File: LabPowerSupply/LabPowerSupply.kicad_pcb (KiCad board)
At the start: 4 copper layers, 203 parts, among them Q1_CP1 FMMT495TA, Q1_CP2 FMMT495TA, Q1_LVR1 PJA3404_R1_00001, Q1_LVR2 PJA3404_R1_00001, Q2_LVR1 PJA3404_R1_00001, Q2_LVR2 PJA3404_R1_00001, Q3_LVR1 PJA3404_R1_00001, Q3_LVR2 PJA3404_R1_00001, Y1 8M, Y2 8M

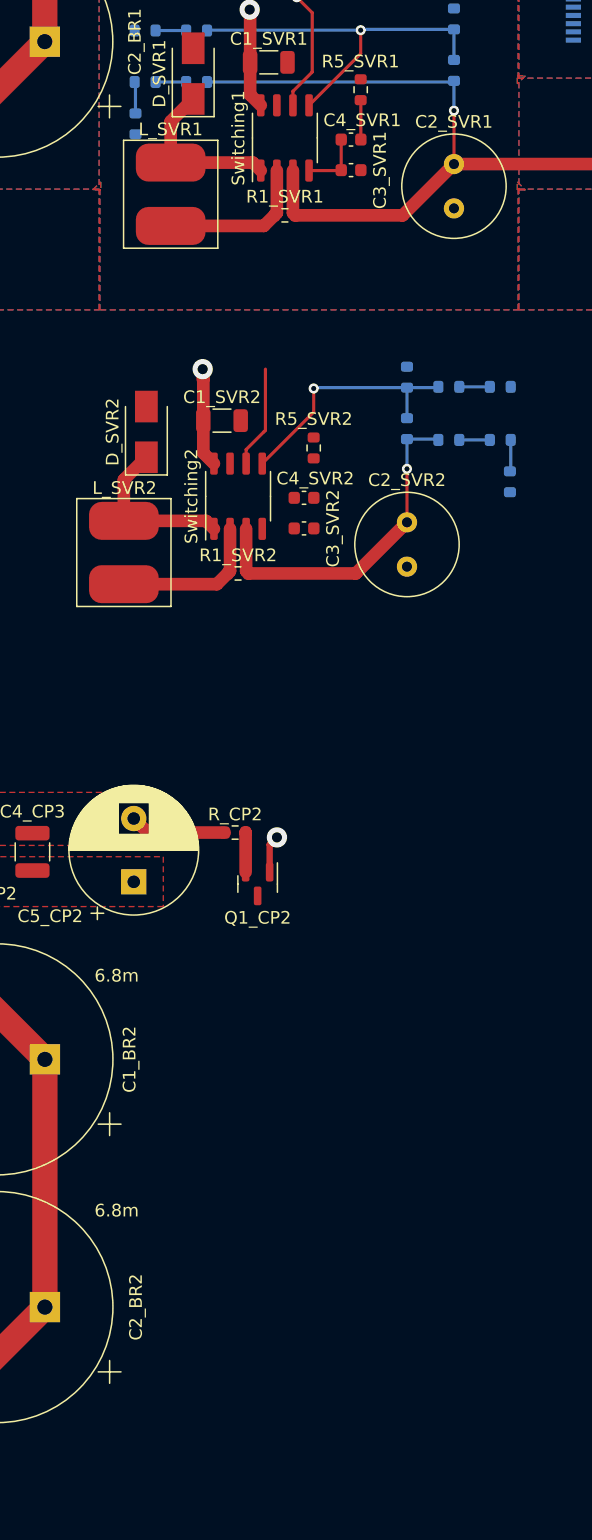
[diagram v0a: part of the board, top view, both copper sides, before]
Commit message: Copied channel module positions other than linear
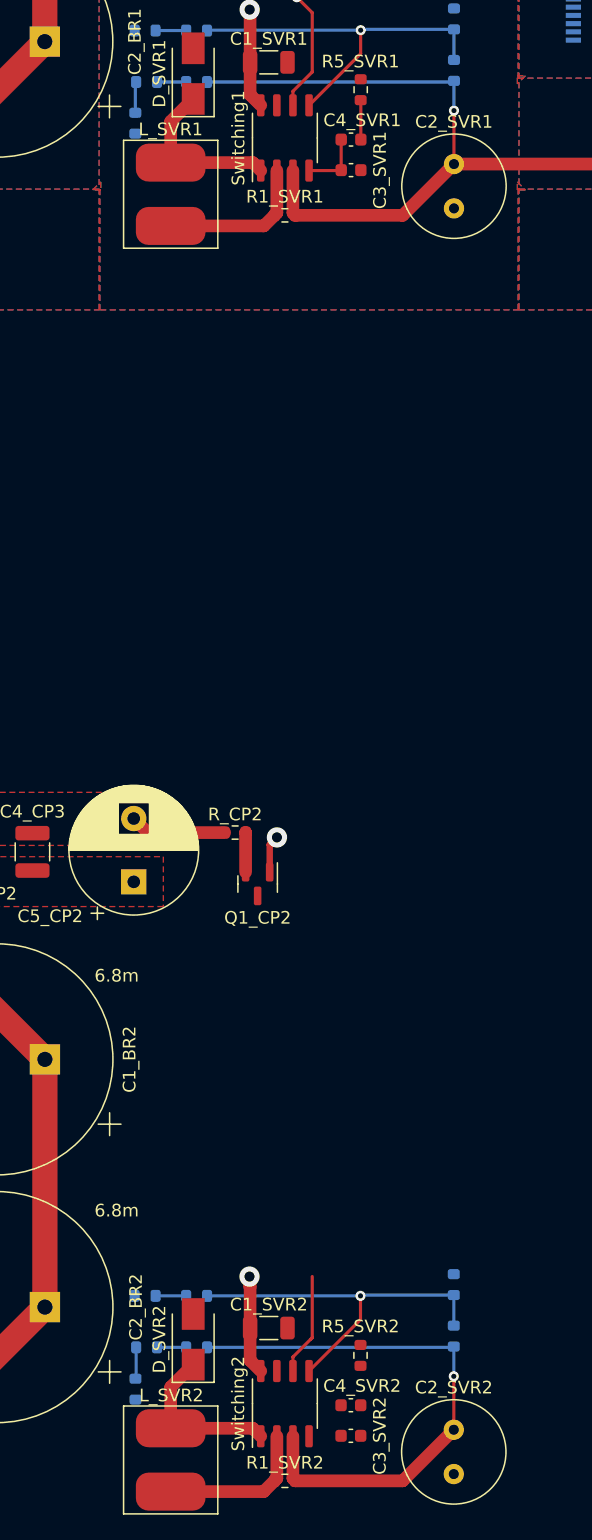
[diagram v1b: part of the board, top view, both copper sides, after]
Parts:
- moved R6_SVR2 77.5 mm to (57.2, 173.5)
- moved R41_SVR2 77.1 mm to (57.9, 166.1), turned to 180 degrees
- moved R32_SVR2 76.9 mm to (58.0, 170.2), turned to 180 degrees
- moved R42_SVR2 74.5 mm to (62.0, 166.1), turned to 180 degrees
- moved R31_SVR2 74.4 mm to (62.0, 170.2), turned to 180 degrees
- moved C1_SVR2 71.7 mm to (67.7, 168.7)
- moved C4_SVR2 71.7 mm to (74.2, 174.8)
- moved R1_SVR2 71.7 mm to (69.0, 180.7)
- moved R7_SVR2 71.7 mm to (82.3, 165.2)
- moved C2_SVR2 71.7 mm to (82.3, 176.7)
- moved C3_SVR2 71.7 mm to (74.2, 177.2)
- moved L_SVR2 71.7 mm to (59.9, 179.1)
- moved R2_SVR2 71.7 mm to (82.3, 169.3)
- moved R5_SVR2 71.7 mm to (74.9, 170.8)
- moved Switching2 71.7 mm to (69.0, 174.6)
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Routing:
- net /Channel Power Supply 2/Linear Voltage Regulator /Linear Input: track 26.9 -> 43.9 mm
- net /Channel Power Supply 2/Switching Voltage Regulator/FeedBack: track 19.9 -> 29.5 mm

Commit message: Started mcu
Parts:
- moved C10_Power1 169.5 mm to (169.2, 34.4), turned to 90 degrees
- moved C2_Y1 166.6 mm to (185.9, 53.9), turned to 90 degrees
- moved C5_Power1 166.5 mm to (172.1, 34.4), turned to 90 degrees
- moved R11_OA2 163.1 mm to (80.4, 154.8)
- moved R12_OA2 163.1 mm to (64.3, 154.8)
- moved R13_OA2 163.1 mm to (63.5, 158.1)
- moved R2_OA2 163.1 mm to (64.3, 152.3)
- moved R51_OA2 163.1 mm to (69.9, 145.9)
- moved OpAmp2 163.1 mm to (72.3, 153.5)
- moved R10_OA2 163.1 mm to (82.2, 139.3)
- moved R4_OA2 163.1 mm to (74.6, 146.7)
- moved R52_OA2 163.1 mm to (69.0, 142.1)
- moved R6_OA2 163.1 mm to (65.0, 142.1)
- moved R7_OA2 163.1 mm to (78.4, 150.1)
- moved R8_OA2 163.1 mm to (75.5, 143.4)
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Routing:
- net +3.3V: track 4.22 -> 45.8 mm
- net GND1: track 17.5 -> 57.7 mm
- net Net-(C1_Y1-Pad2): track 0.00 -> 18.6 mm
- net Net-(C2_Y1-Pad2): track 0.00 -> 11.0 mm
- net Net-(J_Boot1-Pad2): track 0.00 -> 10.3 mm
- net Net-(J_Boot1-Pad1): track 0.00 -> 4.21 mm
- net Net-(J_Boot1-Pad3): track 0.00 -> 3.69 mm

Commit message: Fixed MCU communication pins and optocoupler
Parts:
- added R_I2C1: 4.7k, Resistor_SMD:R_0603_1608Metric, B.Cu at (199.9, 34.8)
- added R_I2C2: 4.7k, Resistor_SMD:R_0603_1608Metric, B.Cu at (199.9, 32.3)
- added R_OPT1: 470, Resistor_SMD:R_0603_1608Metric, F.Cu at (337.4, 30.2)
- added R_OPT2: 470, Resistor_SMD:R_0603_1608Metric, F.Cu at (329.4, 30.2)
- added R_OPT3: 10k, Resistor_SMD:R_0603_1608Metric, F.Cu at (329.4, 27.7)
- added R_OPT4: 10k, Resistor_SMD:R_0603_1608Metric, F.Cu at (337.4, 27.7)
- added R_OPT5: 10k, Resistor_SMD:R_0603_1608Metric, F.Cu at (333.4, 27.7)
- added R_OPT6: 10k, Resistor_SMD:R_0603_1608Metric, F.Cu at (333.4, 30.2)
- added R_USB1: 22, Resistor_SMD:R_0603_1608Metric, B.Cu at (270.3, 22.9)
- added R_USB2: 22, Resistor_SMD:R_0603_1608Metric, B.Cu at (270.3, 20.1)
- J_STLink1: value Conn_01x05_Male -> Conn_01x06_Male; footprint Connector_PinHeader_2.54mm:PinHeader_1x05_P2.54mm_Vertical -> Connector_PinHeader_2.54mm:PinHeader_1x06_P2.54mm_Vertical
- R_CC1, R_CC2: value 4.7k -> 5.1k
- moved D_LVR2 177.4 mm to (94.2, 144.1), turned to 180 degrees
- moved R4_LVR2 175.5 mm to (102.9, 67.6)
- moved C3_LVR2 175.4 mm to (101.5, 156.0), turned to -90 degrees
- moved Q3_LVR2 172.3 mm to (104.0, 161.3)
- moved Linear1_2 171.5 mm to (109.3, 142.0)
- moved Linear2 171.5 mm to (105.9, 155.9)
- moved C1_LVR2 171.3 mm to (117.7, 145.8), turned to 180 degrees
- moved R3_LVR2 170.5 mm to (98.6, 155.8)
- moved C4_LVR2 170.3 mm to (103.1, 142.7), turned to 180 degrees
- moved R13_LVR2 167.6 mm to (102.1, 171.6), turned to 0 degrees
- moved Inverter2 164.9 mm to (95.2, 165.0)
- moved R12_LVR2 163.0 mm to (107.1, 145.7)
- moved Q1_LVR2 161.5 mm to (94.8, 149.4), turned to 180 degrees
- moved Q2_LVR2 161.5 mm to (99.6, 149.6)
- moved R11_LVR2 160.0 mm to (103.1, 145.7)
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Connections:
- net /Primary Controller/Reset renamed Net-(MCU_1-Pad7)
- Front_Panel1 pad 1: +3.3V -> GND1
- Front_Panel1 pad 15: Net-(Front_Panel1-Pad15) -> GND1
- Front_Panel1 pad 2: Net-(Front_Panel1-Pad2) -> unconnected-(Front_Panel1-Pad2)
- Front_Panel1 pad 3: Net-(Front_Panel1-Pad3) -> Net-(MCU_1-Pad25)
- Front_Panel1 pad 4: Net-(Front_Panel1-Pad4) -> Net-(MCU_1-Pad26)
- Front_Panel1 pad 5: GND1 -> Net-(MCU_1-Pad27)
- Front_Panel1 pad 7: Net-(Front_Panel1-Pad7) -> Net-(MCU_1-Pad29)
- Inverter2 pad 3: Net-(Inverter2-Pad3) -> (no net)
- Inverter2 pad 4: /Optocouplers/RX 2 -> (no net)
- Inverter2 pad 5: /Optocouplers/TX 2 -> (no net)
- Inverter2 pad 6: Net-(Inverter2-Pad6) -> (no net)
- J_STLink1 pad 2: GND1 -> /Primary Controller/SW_CLK
- J_STLink1 pad 3: /Primary Controller/SWDIO -> GND1
- J_STLink1 pad 4: /Primary Controller/SWCLK -> /Primary Controller/SW_DIO
- MCU_1 pad 25: unconnected-(MCU_1-Pad25) -> Net-(MCU_1-Pad25)
- MCU_1 pad 26: Net-(Front_Panel1-Pad2) -> Net-(MCU_1-Pad26)
- MCU_1 pad 27: Net-(Front_Panel1-Pad3) -> Net-(MCU_1-Pad27)
- MCU_1 pad 28: Net-(Front_Panel1-Pad4) -> Net-(Front_Panel1-Pad6)
- MCU_1 pad 29: Net-(Front_Panel1-Pad16) -> Net-(MCU_1-Pad29)
- MCU_1 pad 30: Net-(Front_Panel1-Pad15) -> Net-(Front_Panel1-Pad8)
- MCU_1 pad 33: Net-(Front_Panel1-Pad14) -> Net-(Front_Panel1-Pad9)
- MCU_1 pad 34: Net-(Front_Panel1-Pad13) -> Net-(Front_Panel1-Pad10)
- MCU_1 pad 35: Net-(Front_Panel1-Pad12) -> Net-(Front_Panel1-Pad11)
- MCU_1 pad 37: Net-(Front_Panel1-Pad11) -> Net-(Front_Panel1-Pad12)
- MCU_1 pad 38: Net-(Front_Panel1-Pad10) -> Net-(Front_Panel1-Pad13)
- MCU_1 pad 39: Net-(Front_Panel1-Pad9) -> Net-(Front_Panel1-Pad14)
- MCU_1 pad 40: Net-(Front_Panel1-Pad8) -> Net-(Front_Panel1-Pad16)
- MCU_1 pad 44: Net-(J_USB1-PadA7) -> Net-(MCU_1-Pad44)
- MCU_1 pad 45: Net-(J_USB1-PadA6) -> Net-(MCU_1-Pad45)
- MCU_1 pad 46: /Primary Controller/SWDIO -> /Primary Controller/SW_DIO
- MCU_1 pad 49: /Primary Controller/SWCLK -> /Primary Controller/SW_CLK
- MCU_1 pad 55: Net-(Front_Panel1-Pad6) -> /Primary Controller/SWO
- MCU_1 pad 56: Net-(Front_Panel1-Pad7) -> unconnected-(MCU_1-Pad56)
- Optocoupler1 pad 2: /Optocouplers/TX1 -> Net-(Optocoupler1-Pad2)
- Optocoupler1 pad 3: GND1 -> /Optocouplers/TX1
- Optocoupler1 pad 6: Net-(Inverter2-Pad3) -> /Optocouplers/RX 2
- Optocoupler2 pad 2: Net-(Inverter2-Pad6) -> Net-(Optocoupler2-Pad2)
- Optocoupler2 pad 3: GND2 -> /Optocouplers/TX 2
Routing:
- net Net-(J_USB1-PadA1): track 0.00 -> 19.6 mm
- net /Primary Controller/I2C SDA: track 0.00 -> 17.2 mm
- net /Primary Controller/I2C SCL: track 0.00 -> 16.2 mm
- net GND1: track 57.7 -> 69.4 mm
- net +3.3V: track 45.8 -> 36.0 mm
- net /Primary Controller/SW_CLK: track 0.00 -> 9.33 mm
- net Net-(J_Boot1-Pad2): track 10.3 -> 17.7 mm
- net Net-(J_USB1-PadA5): track 0.00 -> 4.72 mm
- net Net-(J_USB1-PadB5): track 0.00 -> 4.22 mm
- net /Primary Controller/SWO: track 0.00 -> 4.15 mm
- net Net-(J_USB1-PadA7): track 0.00 -> 3.79 mm
- net Net-(J_USB1-PadA6): track 0.00 -> 3.79 mm

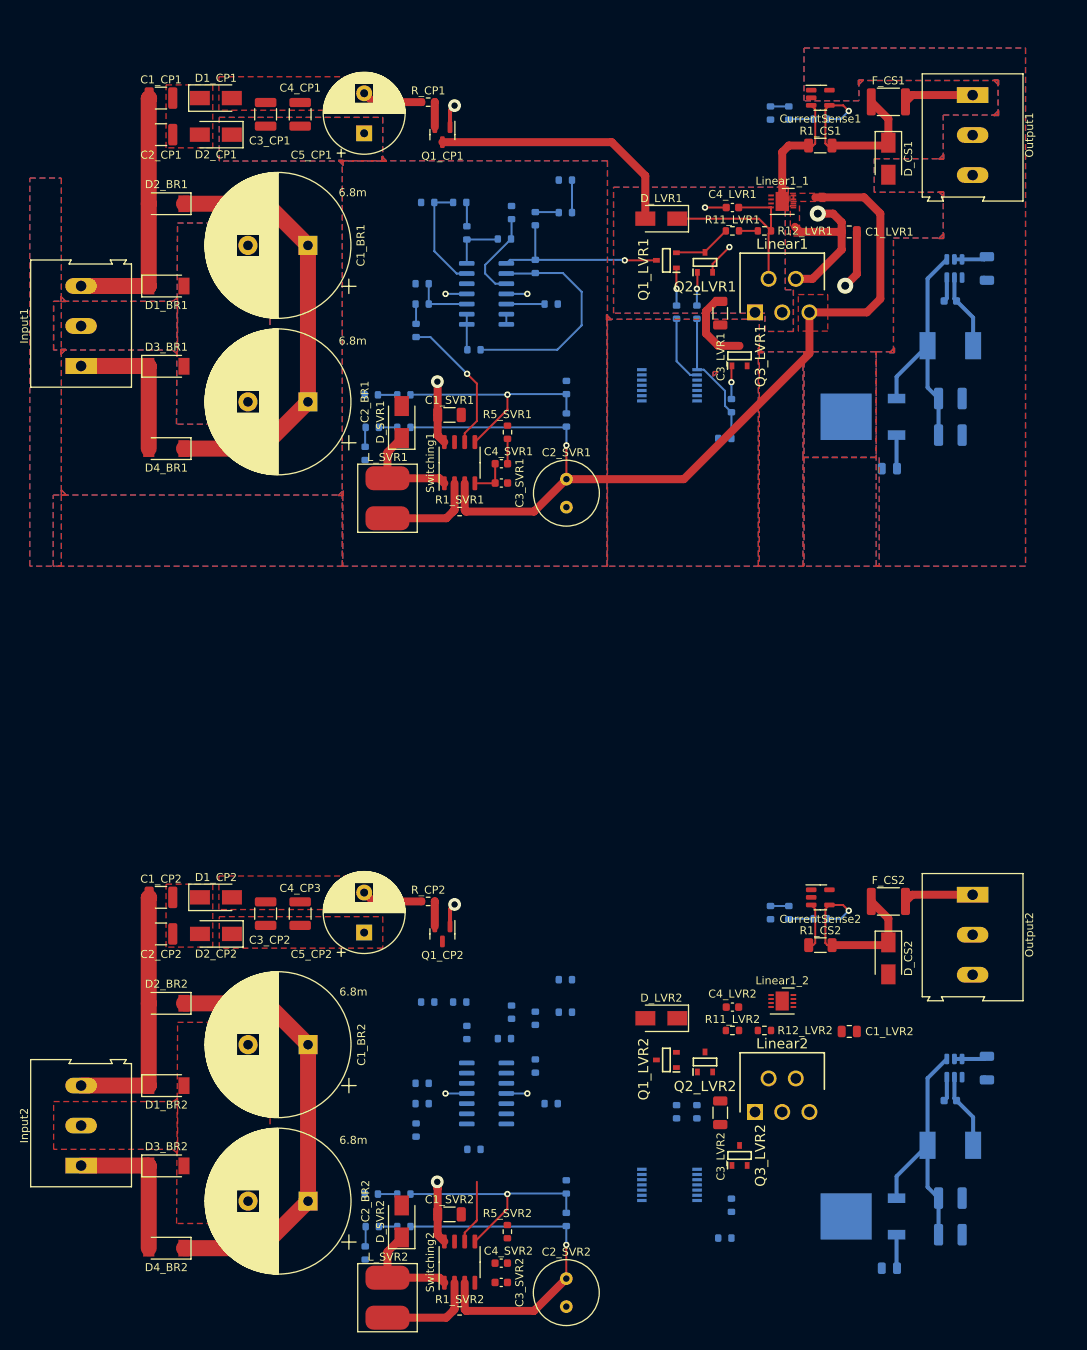
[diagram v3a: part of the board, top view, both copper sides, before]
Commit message: Ground and power planes
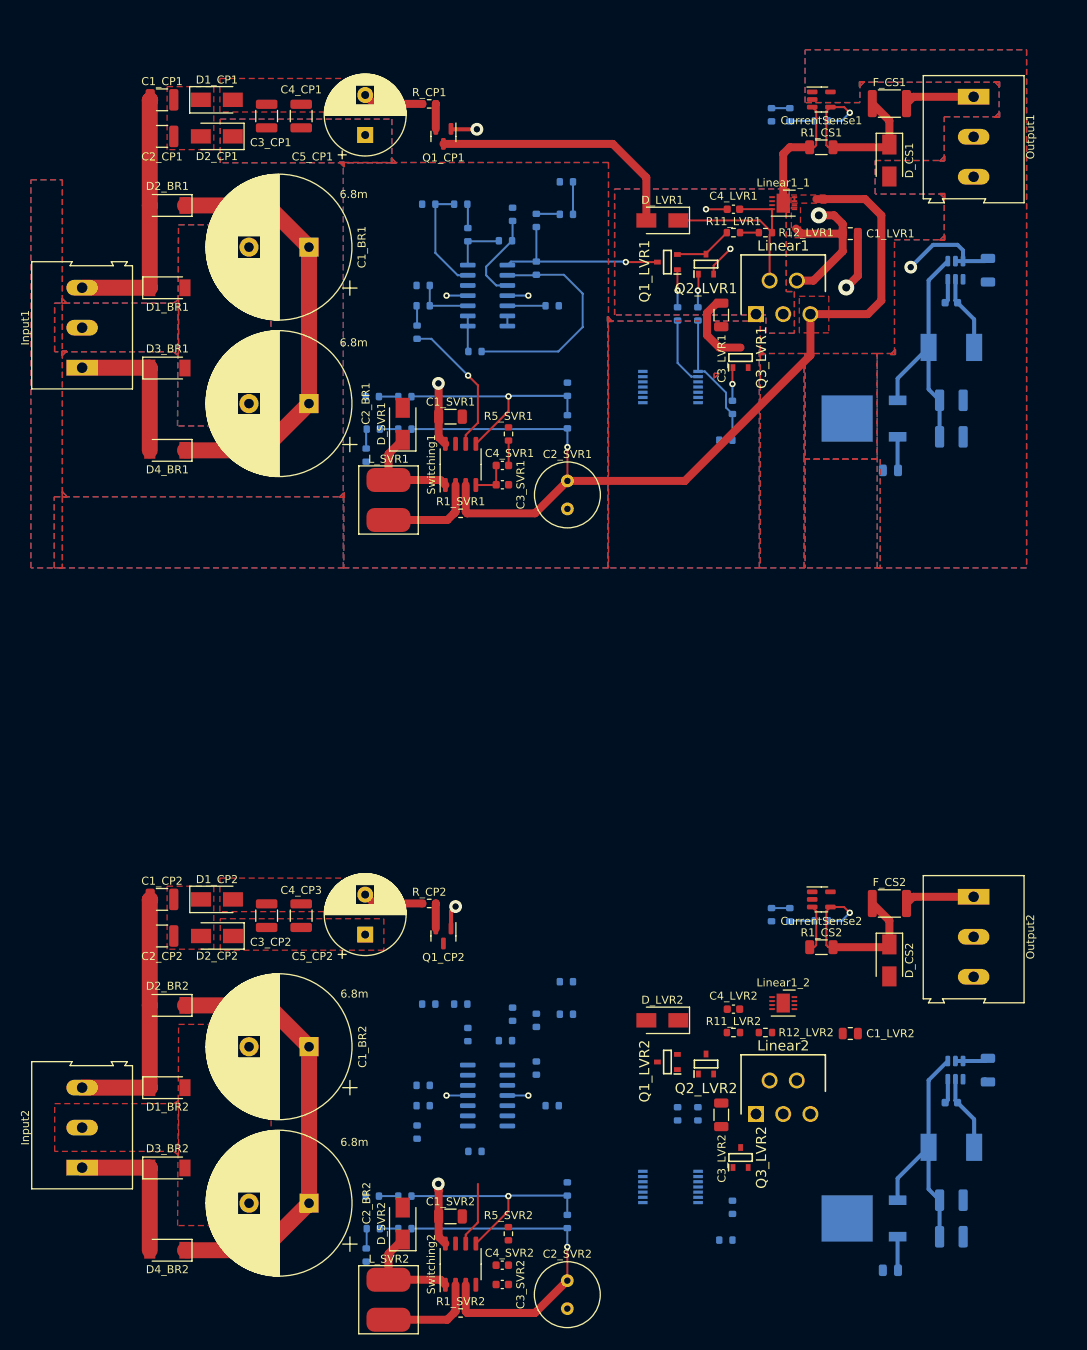
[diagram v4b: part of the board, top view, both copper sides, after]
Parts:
- moved C1_3V2 0.29 mm to (130.4, 171.5)
- moved C1_5V2 0.29 mm to (135.0, 150.6)
- moved C1_LVR2 0.29 mm to (117.8, 146.1)
- moved C2_5V2 0.29 mm to (130.4, 154.7)
- moved C3_5V2 0.29 mm to (130.4, 166.9)
- moved C4_LVR2 0.29 mm to (103.2, 143.0)
- moved L_5V2 0.29 mm to (130.4, 160.3)
- moved Linear1_2 0.29 mm to (109.4, 142.2)
- moved Q1_CP2 0.29 mm to (66.9, 133.9)
- moved Q1_LVR2 0.29 mm to (94.9, 149.6)
- moved R11_LVR2 0.29 mm to (103.2, 145.9)
- moved R11_OA2 0.29 mm to (80.5, 155.1)
- moved R1_CS2 0.29 mm to (114.2, 135.3)
- moved R1_SVR2 0.29 mm to (69.1, 181.0)
- moved R22_CS2 0.29 mm to (110.2, 131.2)
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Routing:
- net VCC: track 90.1 -> 99.4 mm, vias 3 -> 4
- added copper zone on In1.Cu, net /Channel Power Supply 1/Charge Pump/Negative
- added copper zone on In2.Cu, net GND1
- added copper zone on In1.Cu, net VCC

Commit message: Began restructure on ch2
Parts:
- D1_BR2, D2_BR2, D3_BR2, D4_BR2: moved to B.Cu
- moved R4_LVR1 100.0 mm to (103.1, 67.8)
- moved R4_LVR2 88.9 mm to (93.9, 156.2), turned to 0 degrees
- moved R6_OA2 49.2 mm to (111.5, 125.9), turned to 90 degrees
- moved R13_OA2 46.5 mm to (95.5, 124.5), turned to 0 degrees
- moved R2_OA2 45.9 mm to (101.3, 125.2), turned to -90 degrees
- moved R12_OA2 45.5 mm to (98.8, 125.2), turned to -90 degrees
- moved R52_OA2 44.2 mm to (111.5, 129.9), turned to 90 degrees
- moved R51_OA2 40.7 mm to (107.7, 130.8), turned to 0 degrees
- moved R3_OA2 36.6 mm to (93.1, 131.7), turned to -90 degrees
- moved R8_OA2 35.4 mm to (110.2, 136.4), turned to 0 degrees
- moved OpAmp2 34.4 mm to (100.1, 133.3), turned to -90 degrees
- moved R4_OA2 34.2 mm to (106.9, 135.5), turned to -90 degrees
- moved R10_OA2 32.2 mm to (114.3, 143.1), turned to 90 degrees
- moved R6_SVR2 31.5 mm to (84.6, 157.9), turned to 180 degrees
- moved R91_OA2 31.3 mm to (109.5, 139.4), turned to 0 degrees
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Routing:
- net /Channel Power Supply 2/Linear Voltage Regulator /Linear Input: track 43.9 -> 26.5 mm
- net /Channel Power Supply 2/Switching Voltage Regulator/FeedBack: track 29.5 -> 16.2 mm
- net /Channel Power Supply 2/On/Off: track 0.00 -> 8.89 mm
- net Net-(Q1_LVR2-Pad2): track 0.00 -> 8.72 mm
- net Net-(Inverter2-Pad2): track 0.00 -> 8.48 mm
- net VDD: track 69.9 -> 77.4 mm, vias 2 -> 1
- net Net-(C3_SVR2-Pad1): track 0.00 -> 6.99 mm
- net /Channel Power Supply 2/AC 2: track 18.8 -> 13.0 mm
- net Net-(Q1_LVR2-Pad1): track 0.00 -> 4.58 mm, vias 0 -> 1
- net Net-(Q3_LVR2-Pad1): track 0.00 -> 4.55 mm, vias 0 -> 1
- net Net-(Q2_LVR2-Pad1): track 0.00 -> 4.36 mm, vias 0 -> 1
- net Net-(C1_3V2-Pad2): track 32.7 -> 28.7 mm
- net /Channel Power Supply 2/AC 1: track 33.0 -> 36.6 mm
- net Net-(C4_SVR2-Pad2): track 0.00 -> 2.99 mm
- net Net-(R11_LVR2-Pad1): track 0.00 -> 2.35 mm
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- added copper zone on B.Cu, net GND2
